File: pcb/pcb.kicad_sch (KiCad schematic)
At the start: 6 parts, among them J1 USB_C_Receptacle_USB2.0_14P, U1 ATtiny45-20P

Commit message: added pcb
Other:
- added sheet a4988_driver (a4988_driver.kicad_sch)
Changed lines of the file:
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@@
+		)
+	)
+	(sheet
+		(at 184.15 24.13)
+		(size 74.93 41.91)
+		(exclude_from_sim no)
+		(in_bom yes)
+		(on_board yes)
+		(dnp no)
+		(fields_autoplaced yes)
+		(stroke
+			(width 0.1524)
+			(type solid)
+		)
+		(fill
+			(color 0 0 0 0)
+		)
+		(property "Sheetname" "a4988_driver"
+			(at 184.15 23.4184 0)
+			(show_name no)
+			(do_not_autoplace no)
+			(effects
+				(font
+					(size 1.27 1.27)
+				)
+				(justify left bottom)
+			)
+		)
+		(property "Sheetfile" "a4988_driver.kicad_sch"
+			(at 184.15 66.6246 0)
+			(show_name no)
+			(do_not_autoplace no)
+			(effects
+				(font
+					(size 1.27 1.27)
+				)
+				(justify left top)
+			)
+		)
+		(instances
+			(project "pcb"
+				(path "/d87b7c2d-20e2-4e6c-83ca-351ab246585b"
+					(page "2")
+				)
+			)
 		)
 	)

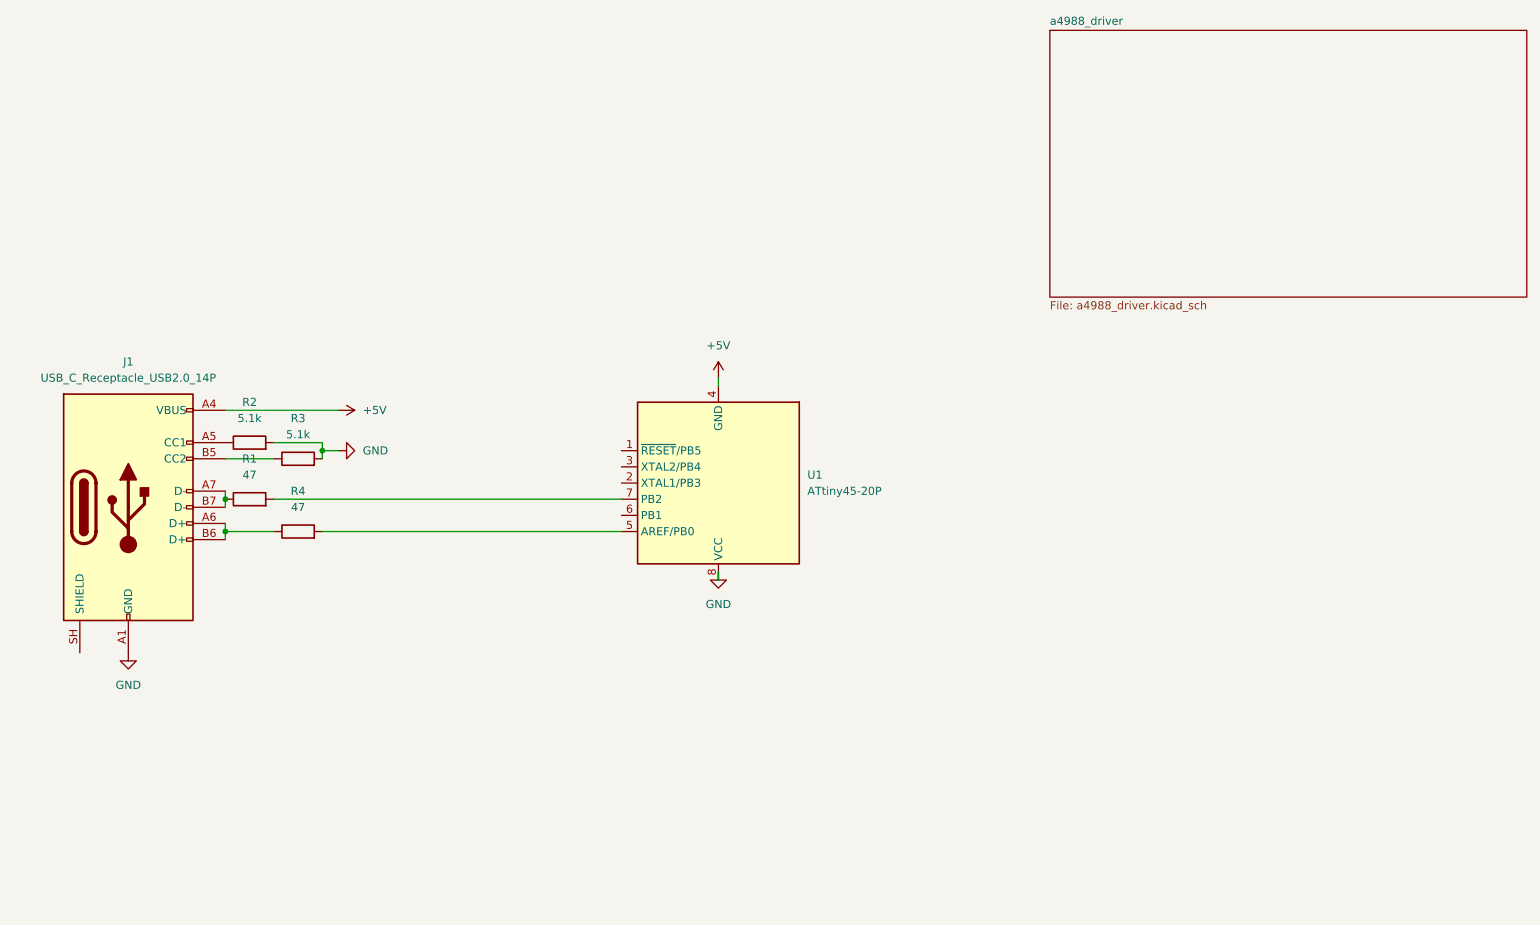
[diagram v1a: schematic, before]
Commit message: added shift register bom and a4988
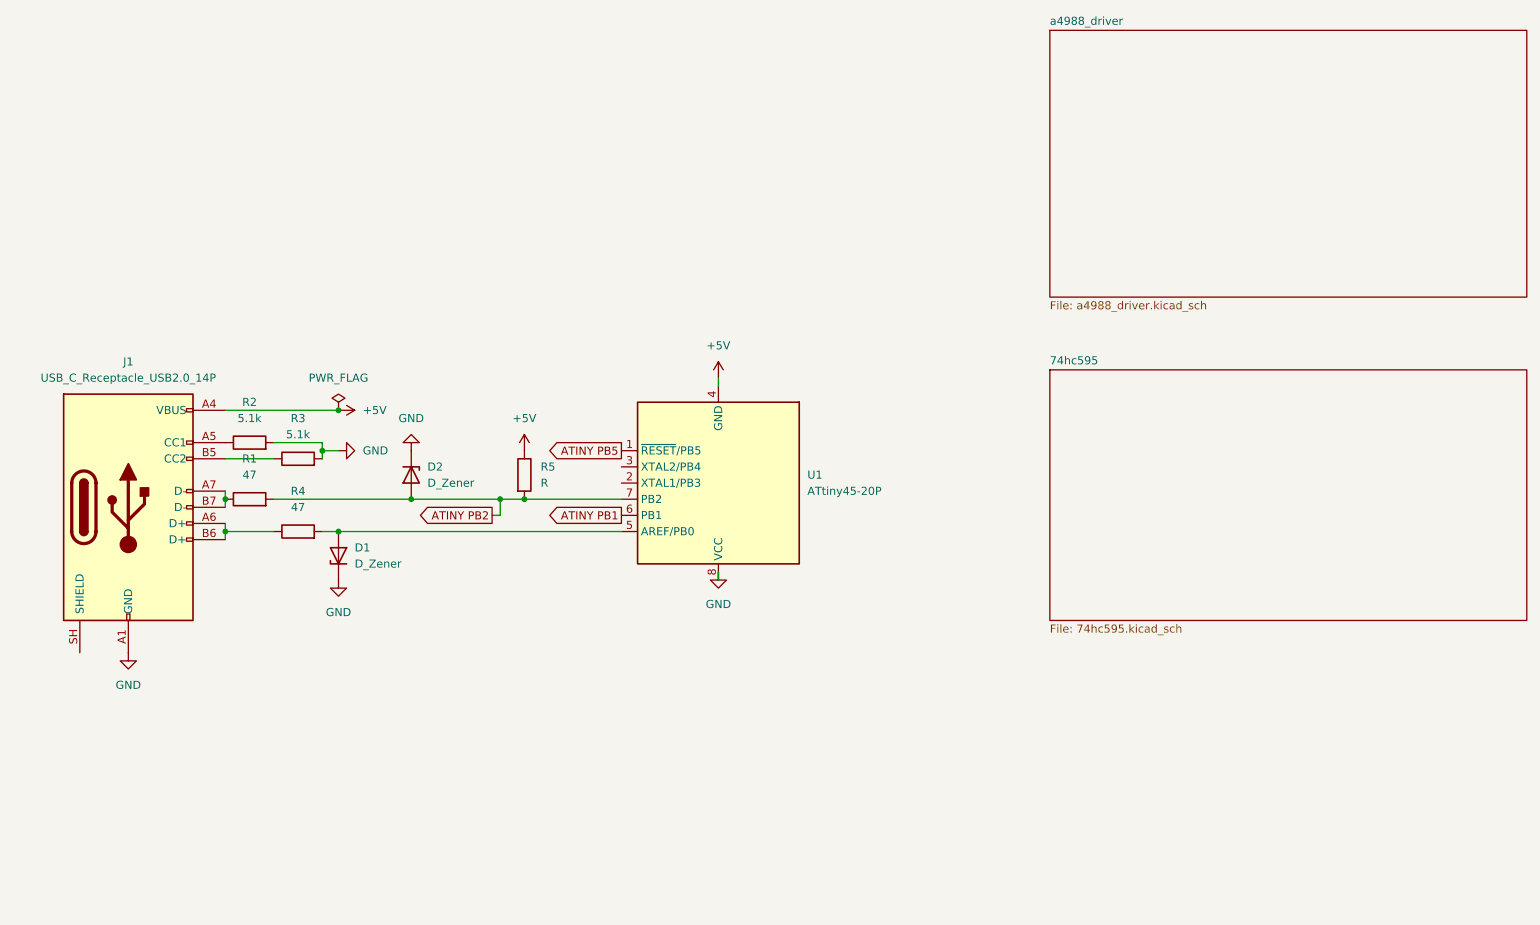
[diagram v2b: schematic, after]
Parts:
- added D1, D2: D_Zener, symbol Device:D_Zener
- added R5: R, symbol Device:R
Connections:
- net +5V: now also R5.1
- net GND: now also D1.1 (K), D2.1 (K)
- net ATINY PB5: now reaches U1.1 (~{RESET}/PB5)
- net at R4.2, U1.5 (AREF/PB0): now also D1.2 (A)
- net ATINY PB1: now reaches U1.6 (PB1)
- net ATINY PB2: now reaches R1.2, U1.7 (PB2)
- net ATINY PB2: now also D2.2 (A), R5.2
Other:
- added sheet 74hc595 (74hc595.kicad_sch)

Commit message: tided schematic
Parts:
- D1, D2: value D_Zener -> 3.6V
- R5: value R -> 1.5k
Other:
- moved on the sheet: D1, D2, J1, R1, R2, R3, R4, R5, U1

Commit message: added journal, and more pcb stuff
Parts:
- removed U1: ATtiny45-20P, Package_DIP:DIP-8_W7.62mm, symbol MCU_Microchip_ATtiny:ATtiny45-20P
- added U5: ATtiny84-20P, Package_DIP:DIP-14_W7.62mm, symbol MCU_Microchip_ATtiny:ATtiny84-20P
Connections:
- net +5V: now also U5.1 (VCC)
- net GND: now also U5.14 (GND)
- net at D1.2 (A), R4.2: now also U5.3 (XTAL2/PB1)
- net ATINY PB2: no longer names the net of D2.2 (A), R1.2, R5.2
- net ATINY PB2: now also U5.2 (XTAL1/PB0)
- new net ATINY PA1: U5.12 (PA1)
- new net ATINY PA2: U5.11 (PA2)
- new net ATINY PA3: U5.10 (PA3)
- new net SCL AS5600: U5.7 (PA6)
- new net SDA AS5600: U5.6 (PA7)
- no-connect marks 0 -> 6
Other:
- added sheet as5600 (as5600.kicad_sch)
